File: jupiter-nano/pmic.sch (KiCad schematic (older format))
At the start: 31 parts, among them U2 ACT8945AQJ305-T

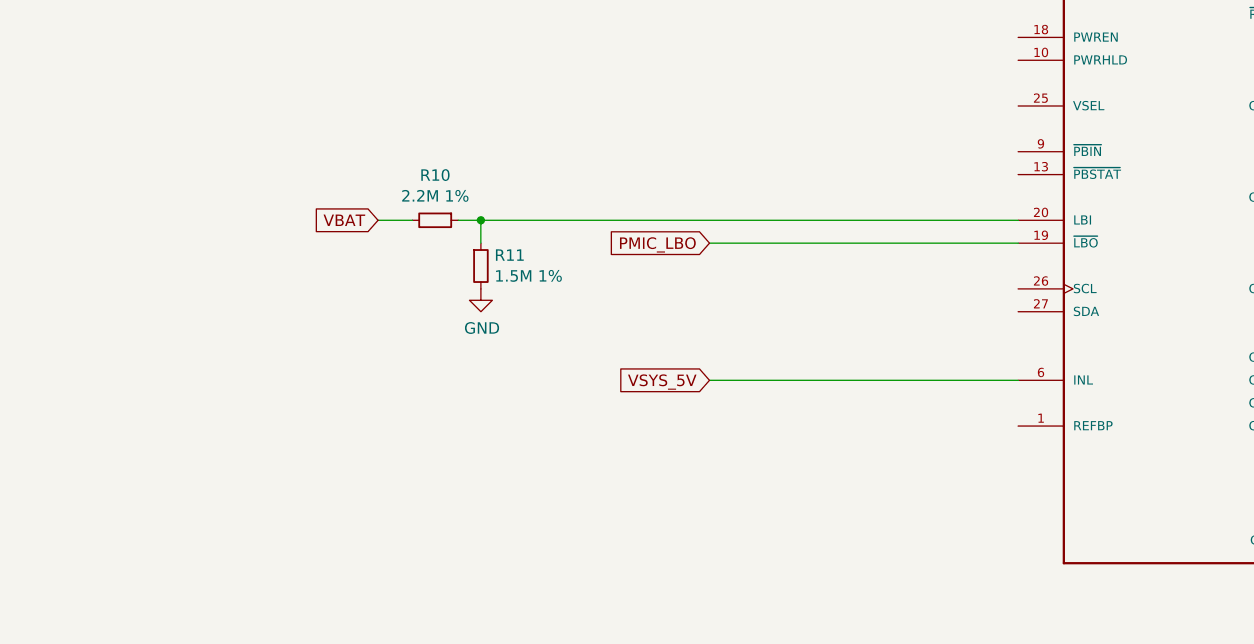
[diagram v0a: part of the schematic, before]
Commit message: PMIC WIP, PBIN and PWRHLD not done
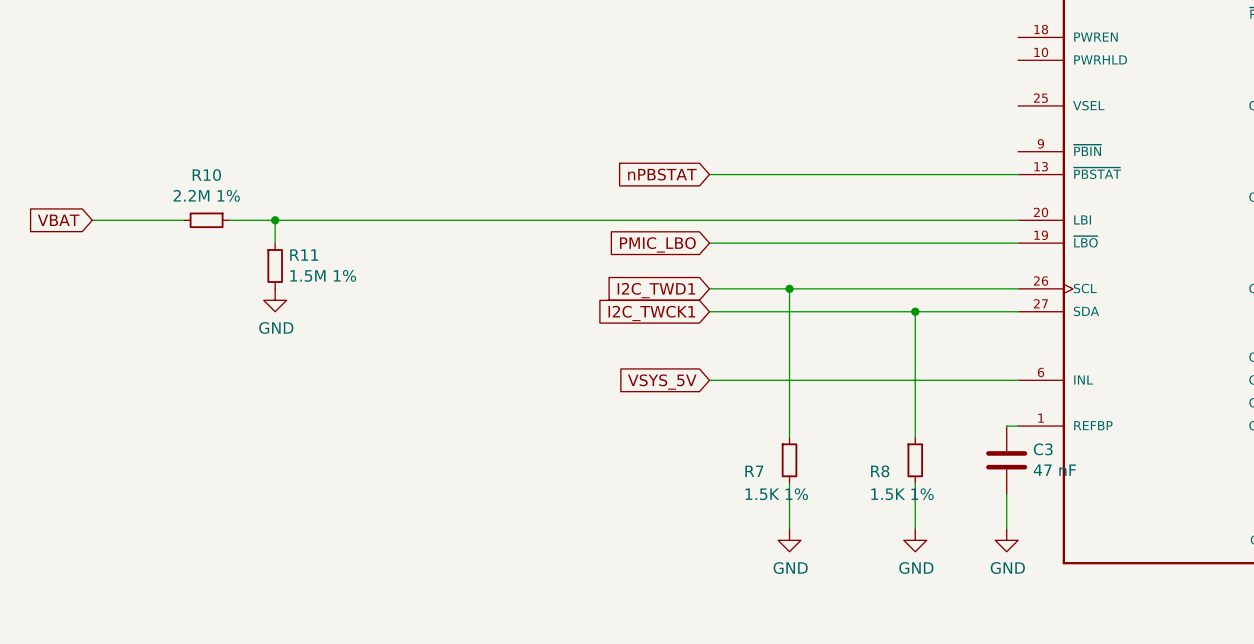
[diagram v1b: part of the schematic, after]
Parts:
- added C3: 47 nF, Capacitor_SMD:C_0201_0603Metric, symbol Device:C
- added R7, R8: 1.5K 1%, Capacitor_SMD:C_0201_0603Metric, symbol Device:R_Small
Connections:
- net GND: now also C3.2, R7.2, R8.2
- net at U2.1 (REFBP): now also C3.1
- net nPBSTAT: now reaches U2.13 (~PBSTAT~)
- net I2C_TWD1: now reaches U2.26 (SCL)
- net I2C_TWD1: now also R7.1
- net I2C_TWCK1: now reaches U2.27 (SDA)
- net I2C_TWCK1: now also R8.1
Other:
- moved on the sheet: R10, R11
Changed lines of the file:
@@
 L Device:R_Small R10
 U 1 1 5F465622
-P 2450 3650
-F 0 "R10" V 2254 3650 50  0000 C CNN
-F 1 "2.2M 1%" V 2345 3650 50  0000 C CNN
-F 2 "Capacitor_SMD:C_0201_0603Metric" H 2450 3650 50  0001 C CNN
-F 3 "~" H 2450 3650 50  0001 C CNN
-	1    2450 3650
+P 1450 3650
+F 0 "R10" V 1254 3650 50  0000 C CNN
+F 1 "2.2M 1%" V 1345 3650 50  0000 C CNN
+F 2 "Capacitor_SMD:C_0201_0603Metric" H 1450 3650 50  0001 C CNN
+F 3 "~" H 1450 3650 50  0001 C CNN
+	1    1450 3650
 	0    1    1    0
 $EndComp
-Text GLabel 2200 3650 0    50   Input ~ 0
+Text GLabel 950  3650 0    50   Input ~ 0
 VBAT
-Wire Wire Line
-	2200 3650 2350 3650
-Wire Wire Line
-	2650 3650 2650 3750
-Connection ~ 2650 3650
-Wire Wire Line
-	2650 3650 2550 3650
 $Comp
 L Device:R_Small R11
 U 1 1 5F467831
-P 2650 3850
-F 0 "R11" H 2709 3896 50  0000 L CNN
-F 1 "1.5M 1%" H 2709 3805 50  0000 L CNN
-F 2 "Capacitor_SMD:C_0201_0603Metric" H 2650 3850 50  0001 C CNN
-F 3 "~" H 2650 3850 50  0001 C CNN
-	1    2650 3850
+P 1750 3850
+F 0 "R11" H 1809 3896 50  0000 L CNN
+F 1 "1.5M 1%" H 1809 3805 50  0000 L CNN
+F 2 "Capacitor_SMD:C_0201_0603Metric" H 1750 3850 50  0001 C CNN
+F 3 "~" H 1750 3850 50  0001 C CNN
+	1    1750 3850
 	1    0    0    -1
 $EndComp
@@
 L power:GND #PWR?
 U 1 1 5F467E51
-P 2650 3950
-F 0 "#PWR?" H 2650 3700 50  0001 C CNN
-F 1 "GND" H 2655 3777 50  0000 C CNN
-F 2 "" H 2650 3950 50  0001 C CNN
-F 3 "" H 2650 3950 50  0001 C CNN
-	1    2650 3950
-	1    0    0    -1
-$EndComp
-Wire Wire Line
-	2650 3650 5000 3650
+P 1750 3950
+F 0 "#PWR?" H 1750 3700 50  0001 C CNN
+F 1 "GND" H 1755 3777 50  0000 C CNN
+F 2 "" H 1750 3950 50  0001 C CNN
+F 3 "" H 1750 3950 50  0001 C CNN
+	1    1750 3950
+	1    0    0    -1
+$EndComp
 Wire Wire Line
 	5000 3750 3650 3750
@@
 	0    -1   -1   0
 $EndComp
+Wire Wire Line
+	5000 4550 4950 4550
+$Comp
+L Device:C C3
+U 1 1 5F5715C5
+P 4950 4700
+F 0 "C3" H 5065 4746 50  0000 L CNN
+F 1 "47 nF" H 5065 4655 50  0000 L CNN
+F 2 "Capacitor_SMD:C_0201_0603Metric" H 4988 4550 50  0001 C CNN
+F 3 "~" H 4950 4700 50  0001 C CNN
+	1    4950 4700
+	1    0    0    -1
+$EndComp
+Wire Wire Line
+	4950 4850 4950 5000
+$Comp
+L power:GND #PWR?
+U 1 1 5F57CB94
+P 4950 5000
+F 0 "#PWR?" H 4950 4750 50  0001 C CNN
+F 1 "GND" H 4955 4827 50  0000 C CNN
+F 2 "" H 4950 5000 50  0001 C CNN
+F 3 "" H 4950 5000 50  0001 C CNN
+	1    4950 5000
+	1    0    0    -1
+$EndComp
+Wire Wire Line
+	950  3650 1350 3650
+Wire Wire Line
+	1550 3650 1750 3650
+Wire Wire Line
+	1750 3750 1750 3650
+Connection ~ 1750 3650
+Wire Wire Line
+	1750 3650 5000 3650
+Wire Wire Line
+	5000 3450 3650 3450
+Text GLabel 3650 3450 0    50   Input ~ 0
+nPBSTAT
+Wire Wire Line
+	5000 3950 4000 3950
+Text GLabel 3650 3950 0    50   Input ~ 0
+I2C_TWD1
+Wire Wire Line
+	5000 4050 4550 4050
+Text GLabel 3650 4050 0    50   Input ~ 0
+I2C_TWCK1
+Wire Wire Line
+	4000 3950 4000 4600
+Connection ~ 4000 3950
+Wire Wire Line
+	4000 3950 3650 3950
+Wire Wire Line
+	4550 4050 4550 4600
+Connection ~ 4550 4050
+Wire Wire Line
+	4550 4050 3650 4050
+$Comp
+L Device:R_Small R7
+U 1 1 5F5D8A0F
+P 4000 4700
+F 0 "R7" H 3800 4650 50  0000 L CNN
+F 1 "1.5K 1%" H 3800 4550 50  0000 L CNN
+F 2 "Capacitor_SMD:C_0201_0603Metric" H 4000 4700 50  0001 C CNN
+F 3 "~" H 4000 4700 50  0001 C CNN
+	1    4000 4700
+	1    0    0    -1
+$EndComp
+$Comp
+L Device:R_Small R8
+U 1 1 5F5D9763
+P 4550 4700
+F 0 "R8" H 4350 4650 50  0000 L CNN
+F 1 "1.5K 1%" H 4350 4550 50  0000 L CNN
+F 2 "Capacitor_SMD:C_0201_0603Metric" H 4550 4700 50  0001 C CNN
+F 3 "~" H 4550 4700 50  0001 C CNN
+	1    4550 4700
+	1    0    0    -1
+$EndComp
+Wire Wire Line
+	4000 4800 4000 5000
+Wire Wire Line
+	4550 4800 4550 5000
+$Comp
+L power:GND #PWR?
+U 1 1 5F5E58C5
+P 4000 5000
+F 0 "#PWR?" H 4000 4750 50  0001 C CNN
+F 1 "GND" H 4005 4827 50  0000 C CNN
+F 2 "" H 4000 5000 50  0001 C CNN
+F 3 "" H 4000 5000 50  0001 C CNN
+	1    4000 5000
+	1    0    0    -1
+$EndComp
+$Comp
+L power:GND #PWR?
+U 1 1 5F5E6EDB
+P 4550 5000
+F 0 "#PWR?" H 4550 4750 50  0001 C CNN
+F 1 "GND" H 4555 4827 50  0000 C CNN
+F 2 "" H 4550 5000 50  0001 C CNN
+F 3 "" H 4550 5000 50  0001 C CNN
+	1    4550 5000
+	1    0    0    -1
+$EndComp
 $EndSCHEMATC

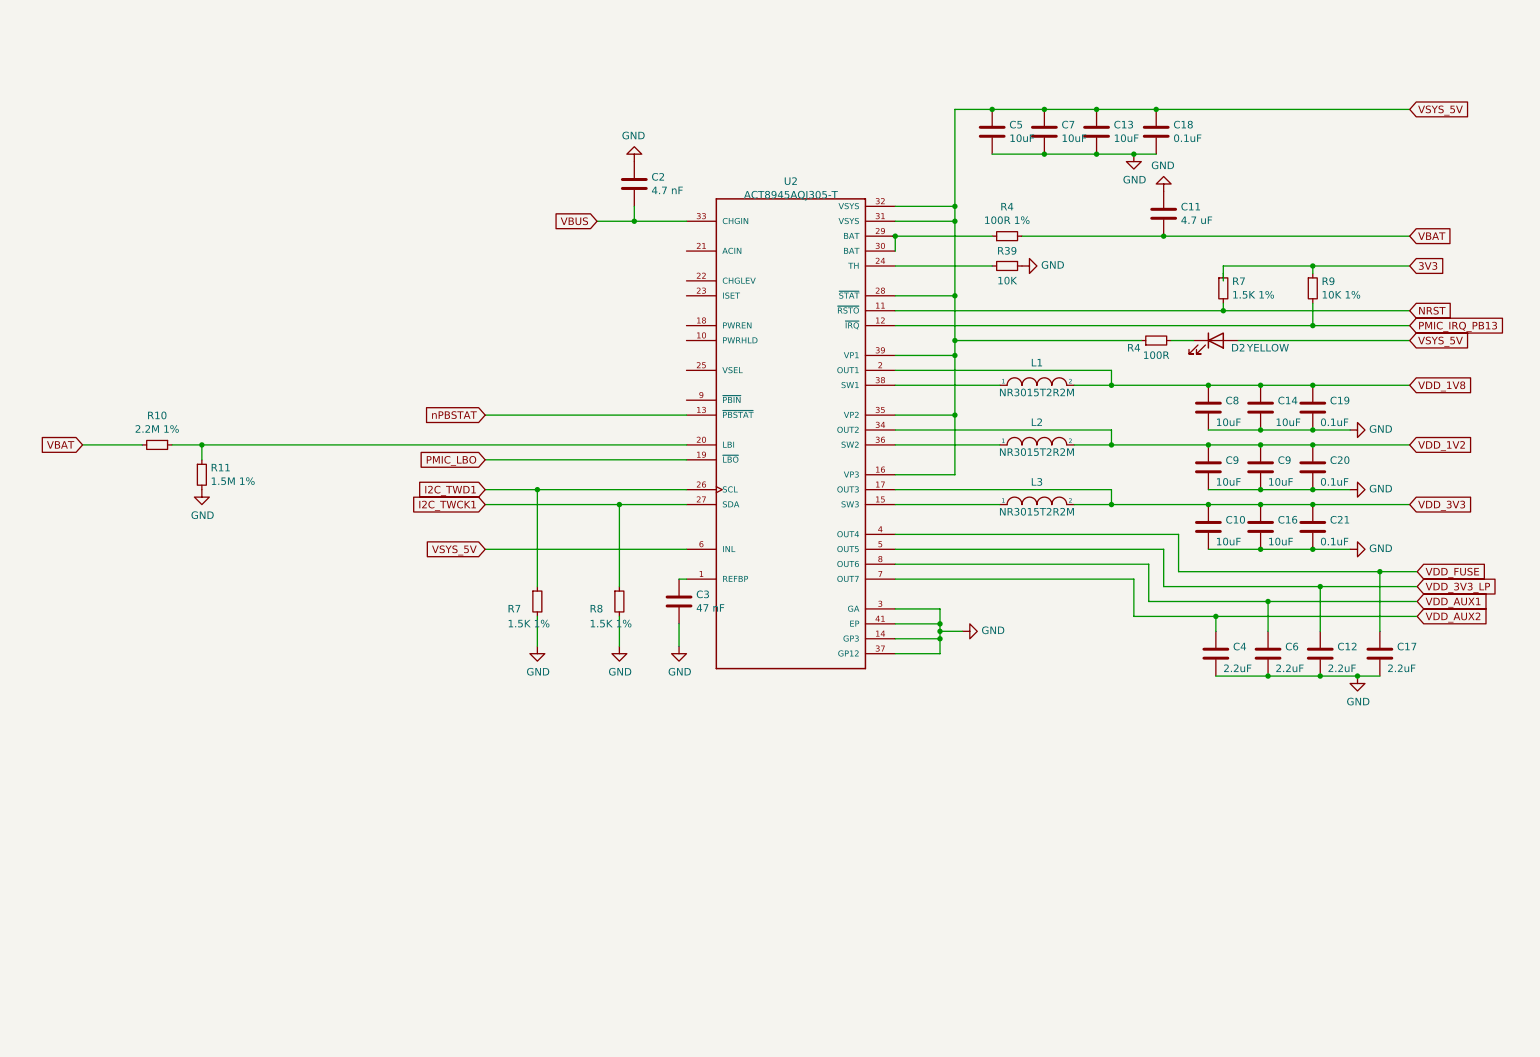
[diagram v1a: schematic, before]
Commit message: WIP, PMIC schematic done
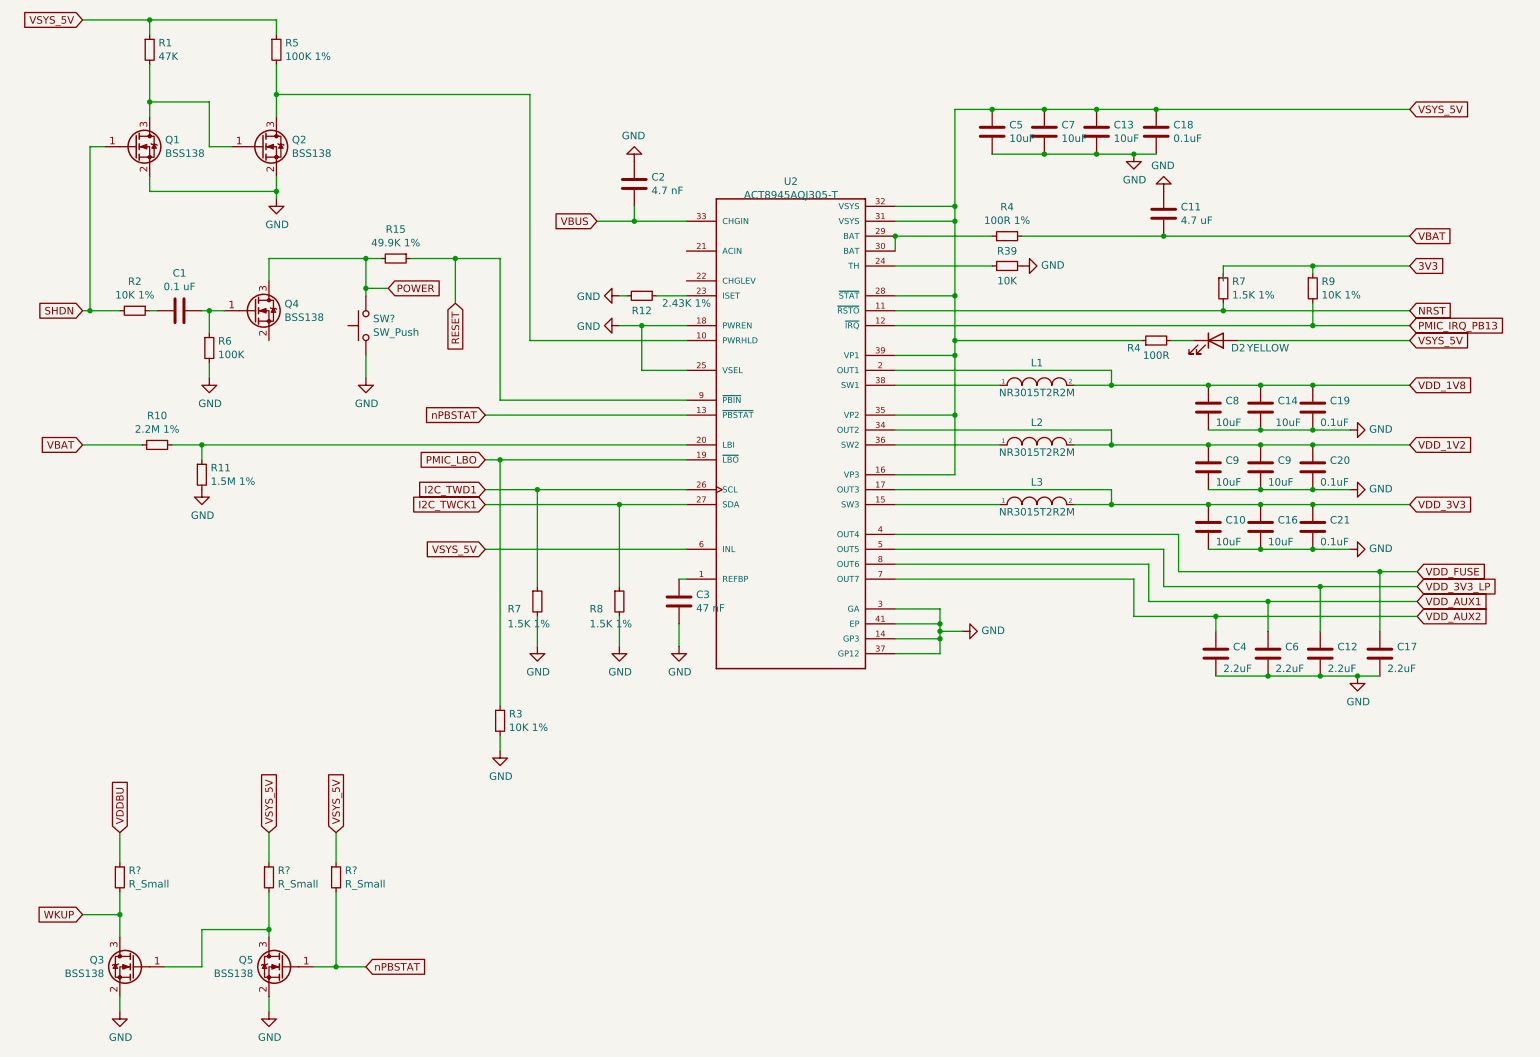
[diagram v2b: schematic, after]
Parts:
- added C1: 0.1 uF, Capacitor_SMD:C_0201_0603Metric, symbol Device:C
- added Q1, Q2, Q3, Q4, Q5: BSS138, Package_TO_SOT_SMD:SOT-23, symbol Transistor_FET:BSS138
- added R1: 47K, Capacitor_SMD:C_0201_0603Metric, symbol Device:R_Small
- added R12: 2.43K 1%, Capacitor_SMD:C_0201_0603Metric, symbol Device:R_Small
- added R15: 49.9K 1%, Capacitor_SMD:C_0201_0603Metric, symbol Device:R_Small
- added R2, R3: 10K 1%, symbol Device:R_Small
- added R5: 100K 1%, Capacitor_SMD:C_0201_0603Metric, symbol Device:R_Small
- added R6: 100K, Capacitor_SMD:C_0201_0603Metric, symbol Device:R_Small
- added R? (x3): R_Small, symbol Device:R_Small
- added SW?: SW_Push, symbol Switch:SW_Push
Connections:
- net GND: now also U2.18 (PWREN), U2.25 (VSEL), Q1.2 (S), Q2.2 (S), Q3.2 (S), Q5.2 (S), R12.2, R3.2, R6.2, SW?.1
- net PMIC_LBO: now also R3.1
- net VSYS_5V: now also R1.1, R5.1, R?.1, R?.1
- net nPBSTAT: now also Q5.1 (G), R?.2
- net at U2.10 (PWRHLD): now also Q2.3 (D), R5.2
- net at U2.23 (ISET): now also R12.1
- net RESET: now reaches U2.9 (~PBIN~)
- net RESET: now also R15.1
- new net: Q3.1 (G), Q5.3 (D), R?.2
- new net: Q1.3 (D), Q2.1 (G), R1.2
- new net: C1.1, Q4.1 (G), R6.1
- new net: C1.2, R2.1
- new net POWER: Q4.3 (D), R15.2, SW?.2
- new net SHDN: Q1.1 (G), R2.2
- new net VDDBU: R?.1
- new net WKUP: Q3.3 (D), R?.2
